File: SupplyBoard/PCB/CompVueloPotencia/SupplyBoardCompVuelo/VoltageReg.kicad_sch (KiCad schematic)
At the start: 4 parts

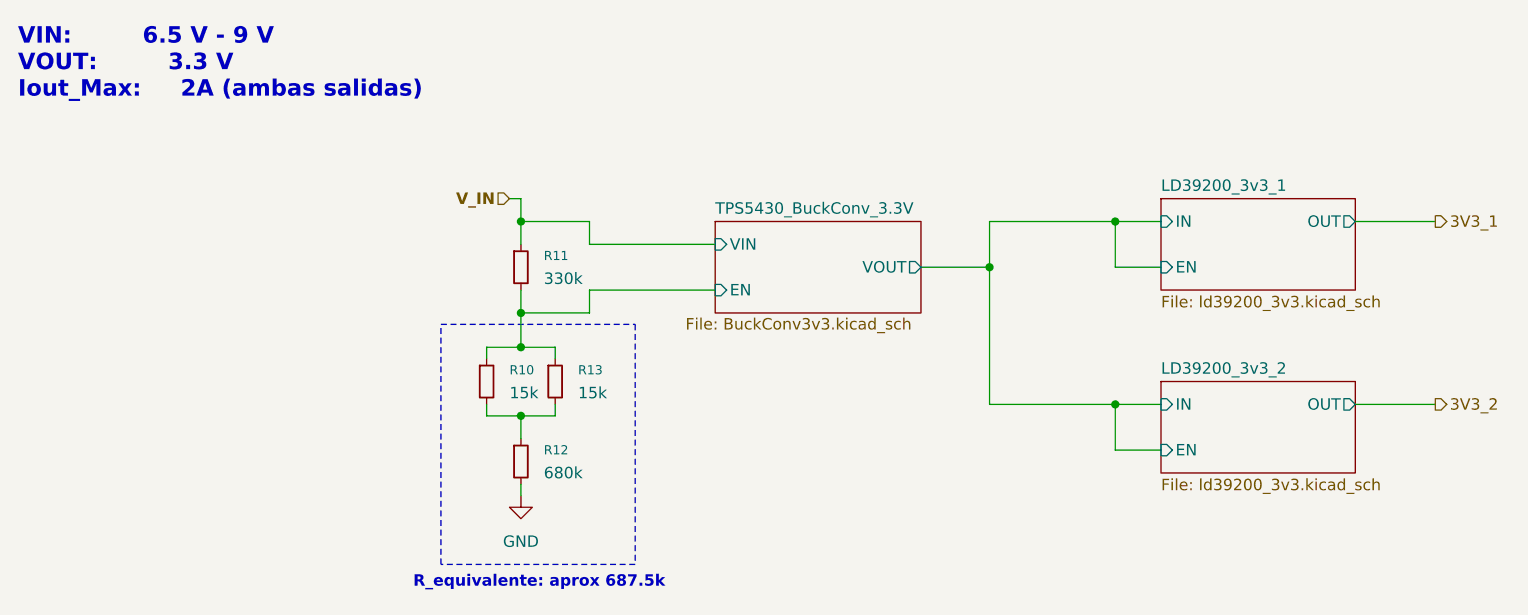
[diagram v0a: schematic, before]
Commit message: Supply Board - Remake Schematic in KiCad 9
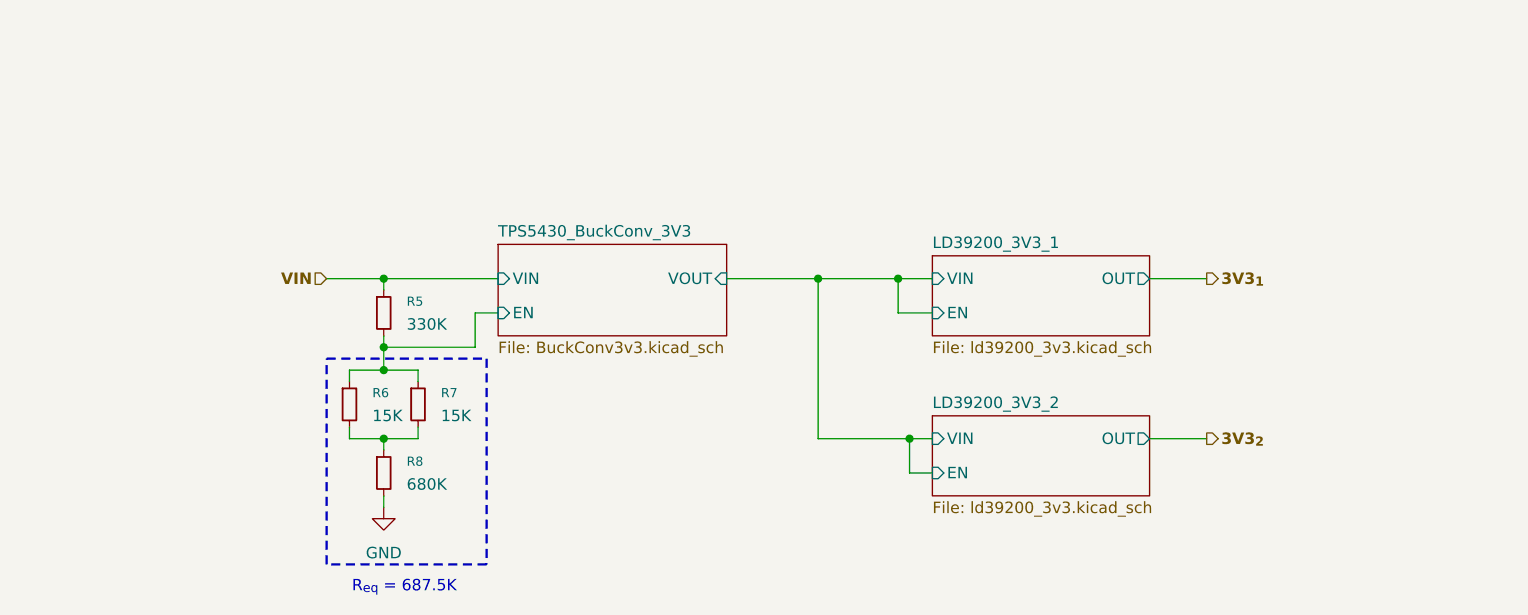
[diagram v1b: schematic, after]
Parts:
- removed R10, R13: 15k, Resistor_SMD:R_0805_2012Metric, symbol Device:R_Small
- removed R11: 330k, Resistor_SMD:R_0805_2012Metric, symbol Device:R_Small
- removed R12: 680k, Resistor_SMD:R_0805_2012Metric, symbol Device:R_Small
- added R5: 330K, symbol Device:R_Small
- added R6, R7: 15K, symbol Device:R_Small
- added R8: 680K, symbol Device:R_Small
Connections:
- net GND: now also R8.2
- new net: R6.2, R7.2, R8.1
- new net TPS5430_BuckConv_3V3/EN: R5.2, R6.1, R7.1
- new net VIN: R5.1
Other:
- removed sheet LD39200_3v3_1
- removed sheet LD39200_3v3_2
- removed sheet TPS5430_BuckConv_3.3V
- added sheet LD39200_3V3_1 (ld39200_3v3.kicad_sch)
- added sheet LD39200_3V3_2 (ld39200_3v3.kicad_sch)
- added sheet TPS5430_BuckConv_3V3 (BuckConv3v3.kicad_sch)
- note added: "R_{eq} = 687.5K"
- note removed: "R_equivalente: aprox 687.5k"
- note removed: "VIN: 6.5 V - 9 V VOUT: 3.3 V Iout_Max: 2A (ambas salidas)"
- company: XIMBAL EK ELECTRONICA -> (none)
